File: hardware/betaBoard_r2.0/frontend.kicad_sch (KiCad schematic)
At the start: 17 parts, among them U5 LM358

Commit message: main r2.0 design done
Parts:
- removed C25: 10p, Capacitor_SMD:C_0603_1608Metric, symbol Device:C
- added C18, C19: 100n, Capacitor_SMD:C_0603_1608Metric, symbol Device:C
- added C20: 1u, Capacitor_SMD:C_0603_1608Metric, symbol Device:C
- added C21: 10p, Capacitor_SMD:C_0603_1608Metric, symbol Device:C
- added D10, D4, D6, D7, D8: ZMM3V3-M, Diode_SMD:D_MiniMELF, symbol Diode:ZMMxx
- added R13, R16, R17: 1k, Resistor_SMD:R_0603_1608Metric, symbol Device:R
- added R14, R15, R18, R20: 10k, Resistor_SMD:R_0603_1608Metric, symbol Device:R
- added R19: 100k, Resistor_SMD:R_0603_1608Metric, symbol Device:R
- added R34: 0, Resistor_SMD:R_0603_1608Metric, symbol Device:R
- added U4: MCP6232, Package_SO:SOIC-8_3.9x4.9mm_P1.27mm, symbol Amplifier_Operational:LM358
- C26: value 10p -> 2p2
- C27: value 470n -> 100n
- C29: value 47p -> 10p
- R21: value 47k -> 1k
- R22: value 150k -> 10k
- R23: value 47M -> 22M
- R24: value 4K7 -> 1k
- R26: value 10k -> 100k
- R27: value 1M -> 100k
- U5: value LM358 -> MCP6232
- renumbered C44 to C45
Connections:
- net Diodes: now also R34.2; no longer R23.2, U5.2 (-)
- net GND: now also C18.2, C20.2, D10.2 (A), D4.2 (A), D6.2 (A), D7.2 (A), D8.2 (A), R15.2, R19.1, U4.4 (V-); no longer R22.2
- net VCC: now also C18.1, R13.1, R16.1, U4.8 (V+)
- net at C26.2, C27.1, R23.1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: now also C19.1, U4.5 (+)
- net at C26.1: now also R23.2, U5.2 (-), R34.1
- net at C45.1, R21.2, U5.3 (+): now also D4.1 (K); no longer R22.1
- net +3V3: no longer names the net of R25.2
- net +3V3: now also D6.1 (K), R13.2
- new net: C19.2, R17.2
- new net: C20.1, R18.1, R19.2, U4.3 (+)
- new net: D8.1 (K), R16.2, R18.2
- new net: C21.1, R17.1, R20.2, U4.2 (-)
- new net: C21.2, R20.1, R22.2, U4.1
- new net: R14.2, U4.6 (-), U4.7
- new net out_dc: D7.1 (K), R14.1, R15.1
- new net out_low_gain: D10.1 (K), R22.1
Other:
- note added: "10pF is the smallest basic component at JLC 10 MOhm the largest R"
- note added: "Biased at 3V => good for ADC"
- note added: "CJ431 Voltage reference as alternative"
- note added: "R = (5V - 3.3V) / 5 mA = 370 Ohm"
- note added: "TODO: Think about voltage reach of OpAmp! TLV272? MCP6232?"
- note removed: "10pF is the smallest basic component at JLC"
- note removed: "Biased at 3V3/2 => good for ADC"
- note removed: "RC-LPF with 1.7 kHz"
- note removed: "RC-LPF with 3.4 kHz"
- note removed: "This is a bit risky: LM358 Datasheet: -> min. 3.3V into 2kOhm with 5V supply Supply voltage is USB - diode_drop - cable_drop -> Probably closer to 4V"
- moved on the sheet: C24, C26, C27, C28, C29, C45, D21, R21, R23, R24, R25, R26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

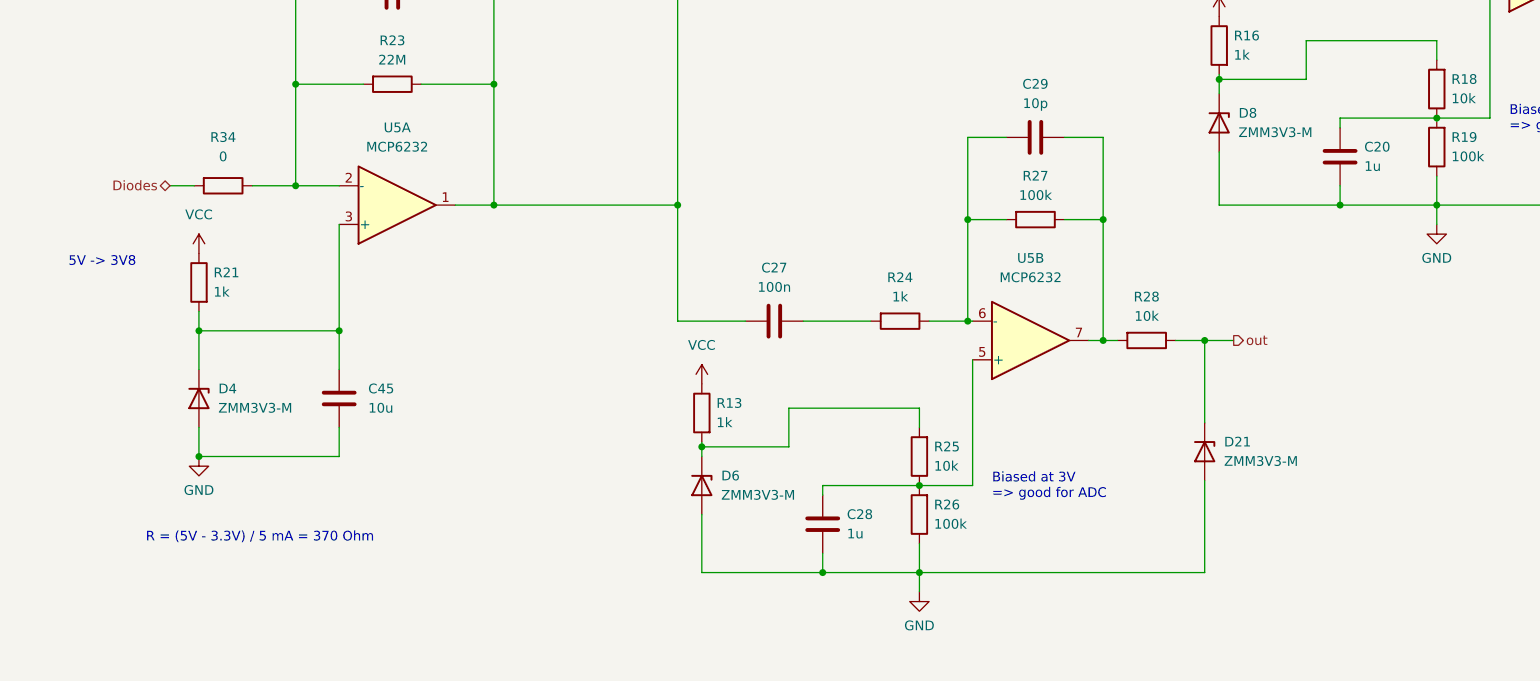
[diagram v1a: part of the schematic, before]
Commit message: hardware: updated kicad version
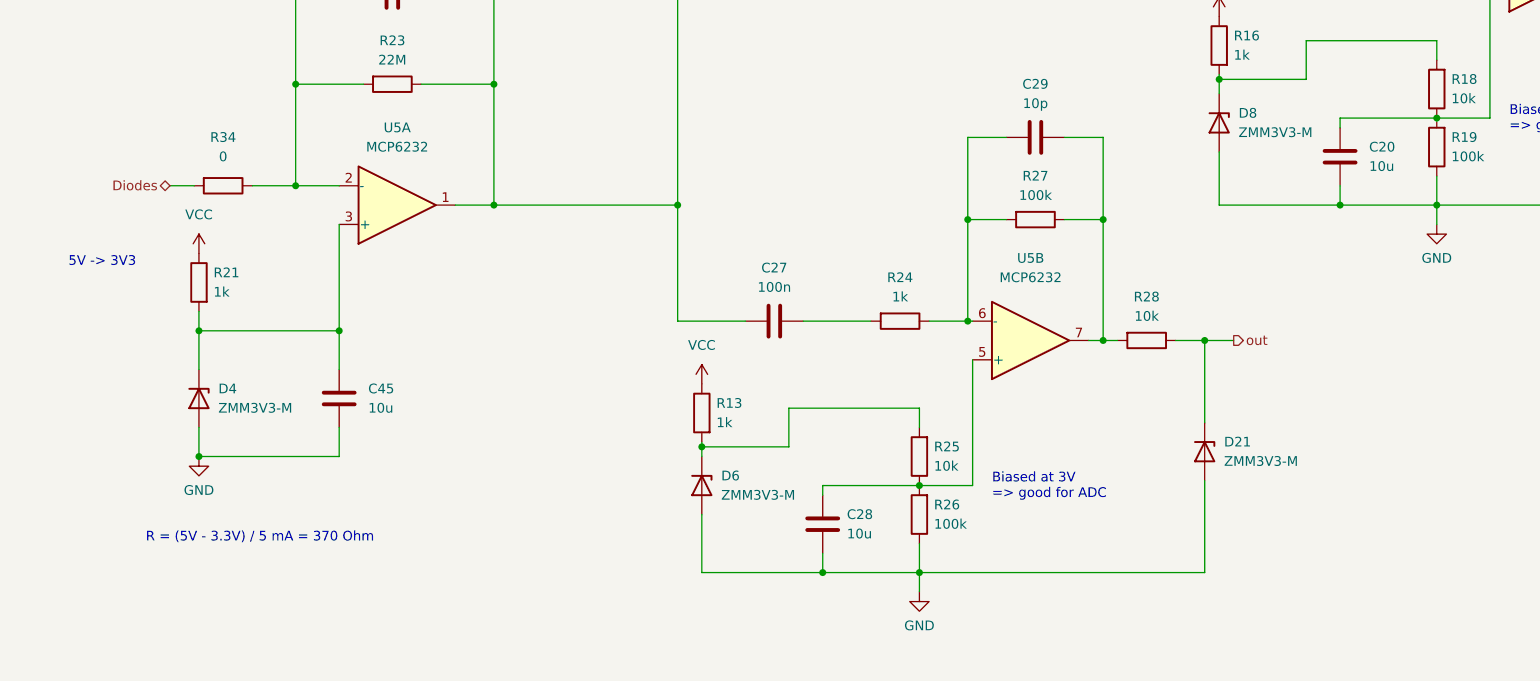
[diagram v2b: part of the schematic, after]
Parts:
- C20, C28: value 1u -> 10u
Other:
- note added: "5V -> 3V3"
- note removed: "5V -> 3V8"
